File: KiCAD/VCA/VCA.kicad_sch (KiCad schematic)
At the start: 14 parts, among them J1 VIN, J2 VC, J3 VOUT, Q1 J172, Q2 J172, U1 LT1006

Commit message: VCA PCB Start
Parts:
- added J4: Conn_01x03_Pin, HackSynth:JST_PH_S3B-PH-K_1x03_P2.00mm_Horizontal, symbol Connector:Conn_01x03_Pin
- C1: footprint (none) -> Capacitor_THT:C_Disc_D5.0mm_W2.5mm_P5.00mm
- R1, R2, R3, R4: value ? -> 10k
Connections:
- net GND: now also J4.1 (Pin_1)
- net VDD: now also C1.1, J4.2 (Pin_2); no longer C1.2
- net VSS: now also C1.2, J4.3 (Pin_3)
- net at Q1.1 (D), R1.2, R3.1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: no longer C1.1
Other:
- note removed: "Is this an error in the original schematic?"
- note removed: "What are the resistor values?"
- moved on the sheet: C1, J1, J2, J3, Q1, Q2, R1, R3, R4, R5, RV1, RV2

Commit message: VCA PCB
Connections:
- net GND: now also J1.S, J2.S, J3.S
- no-connect marks 4 -> 1
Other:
- moved on the sheet: J3
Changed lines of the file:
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@@
+	)
+	(junction
+		(at 93.98 91.44)
+		(diameter 0)
+		(color 0 0 0 0)
+	)
+	(junction
+		(at 196.85 48.26)
+		(diameter 0)
+		(color 0 0 0 0)
 	)
 	(junction
@@
 	)
 	(junction
+		(at 93.98 60.96)
+		(diameter 0)
+		(color 0 0 0 0)
+	)
+	(junction
 		(at 154.94 53.34)
 		(diameter 0)
@@
 	)
 	(no_connect
-		(at 99.06 53.34)
-	)
-	(no_connect
-		(at 176.53 40.64)
-	)
-	(no_connect
-		(at 99.06 83.82)
-	)
-	(no_connect
 		(at 119.38 55.88)
 	)
@@
 	(wire
 		(pts
+			(xy 93.98 91.44) (xy 100.33 91.44)
+		)
+		(stroke
+			(width 0)
+			(type default)
+		)
+	)
+	(wire
+		(pts
+			(xy 167.64 43.18) (xy 191.77 43.18)
+		)
+		(stroke
+			(width 0)
+			(type default)
+		)
+	)
+	(wire
+		(pts
 			(xy 161.29 43.18) (xy 167.64 43.18)
 		)
@@
 	(wire
 		(pts
+			(xy 100.33 83.82) (xy 100.33 91.44)
+		)
+		(stroke
+			(width 0)
+			(type default)
+		)
+	)
+	(wire
+		(pts
 			(xy 191.77 92.71) (xy 191.77 101.6)
 		)
@@
 	(wire
 		(pts
+			(xy 99.06 83.82) (xy 100.33 83.82)
+		)
+		(stroke
+			(width 0)
+			(type default)
+		)
+	)
+	(wire
+		(pts
 			(xy 133.35 43.18) (xy 142.24 43.18)
 		)
@@
 	(wire
 		(pts
+			(xy 190.5 40.64) (xy 190.5 48.26)
+		)
+		(stroke
+			(width 0)
+			(type default)
+		)
+	)
+	(wire
+		(pts
 			(xy 142.24 43.18) (xy 153.67 43.18)
 		)
@@
 	(wire
 		(pts
-			(xy 167.64 43.18) (xy 176.53 43.18)
-		)
-		(stroke
-			(width 0)
-			(type default)
-		)
-	)
-	(wire
-		(pts
 			(xy 133.35 43.18) (xy 129.54 43.18)
 		)
@@
 	(wire
 		(pts
+			(xy 93.98 60.96) (xy 100.33 60.96)
+		)
+		(stroke
+			(width 0)
+			(type default)
+		)
+	)
+	(wire
+		(pts
 			(xy 154.94 76.2) (xy 154.94 73.66)
 		)
@@
 	(wire
 		(pts
-			(xy 181.61 48.26) (xy 181.61 52.07)
+			(xy 196.85 48.26) (xy 196.85 52.07)
 		)
 		(stroke
@@
 	(wire
 		(pts
+			(xy 99.06 53.34) (xy 100.33 53.34)
+		)
+		(stroke
+			(width 0)
+			(type default)
+		)
+	)
+	(wire
+		(pts
+			(xy 190.5 48.26) (xy 196.85 48.26)
+		)
+		(stroke
+			(width 0)
+			(type default)
+		)
+	)
+	(wire
+		(pts
 			(xy 104.14 43.18) (xy 104.14 55.88)
 		)
@@
 	(wire
 		(pts
+			(xy 191.77 40.64) (xy 190.5 40.64)
+		)
+		(stroke
+			(width 0)
+			(type default)
+		)
+	)
+	(wire
+		(pts
 			(xy 181.61 82.55) (xy 181.61 101.6)
+		)
+		(stroke
+			(width 0)
+			(type default)
+		)
+	)
+	(wire
+		(pts
+			(xy 100.33 53.34) (xy 100.33 60.96)
 		)
 		(stroke
@@
 	(symbol
 		(lib_id "power:GND")
-		(at 181.61 52.07 0)
+		(at 196.85 52.07 0)
 		(mirror y)
 		(unit 1)
@@
 		(fields_autoplaced yes)
 		(property "Reference" "#PWR09"
-			(at 181.61 58.42 0)
+			(at 196.85 58.42 0)
 			(effects
 				(font
@@
 		)
 		(property "Value" "GND"
-			(at 181.61 57.15 0)
+			(at 196.85 57.15 0)
 			(effects
 				(font
@@
 		)
 		(property "Footprint" ""
-			(at 181.61 52.07 0)
+			(at 196.85 52.07 0)
 			(effects
 				(font
@@
 		)
 		(property "Datasheet" ""
-			(at 181.61 52.07 0)
+			(at 196.85 52.07 0)
 			(effects
 				(font
@@
 		)
 		(property "Description" "Power symbol creates a global label with name \"GND\" , ground"
-			(at 181.61 52.07 0)
+			(at 196.85 52.07 0)
 			(effects
 				(font
@@
 	(symbol
 		(lib_id "HackSynth:AudioJack2_Ground")
-		(at 181.61 43.18 0)
+		(at 196.85 43.18 0)
 		(mirror y)
 		(unit 1)
@@
 		(dnp no)
 		(property "Reference" "J3"
-			(at 186.69 37.4649 0)
+			(at 201.93 37.4649 0)
 			(effects
 				(font
@@
 		)
 		(property "Value" "VOUT"
-			(at 186.69 43.8149 0)
+			(at 201.93 43.8149 0)
 			(effects
 				(font
@@
 		)
 		(property "Footprint" "HackSynth:Jack_3.5mm"
-			(at 181.61 43.18 0)
+			(at 196.85 43.18 0)
 			(effects
 				(font
@@
 		)
 		(property "Datasheet" "~"
-			(at 181.61 43.18 0)
+			(at 196.85 43.18 0)
 			(effects
 				(font
@@
 		)
 		(property "Description" "Audio Jack, 2 Poles (Mono / TS), Grounded Sleeve"
-			(at 181.61 43.18 0)
-			(effects
-				(font
+			(at 196.85 43.18 0)
+			(effects
+				(font

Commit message: VCA Footprint update
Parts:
- U1: footprint Package_DIP:DIP-8_W7.62mm -> HackSynth:DIP-8_W7.62mm_LongPads
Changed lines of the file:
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@@
 			)
 		)
-		(property "Footprint" "Package_DIP:DIP-8_W7.62mm"
+		(property "Footprint" "HackSynth:DIP-8_W7.62mm_LongPads"
 			(at 154.94 68.58 0)
 			(effects

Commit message: Backup Cleanup
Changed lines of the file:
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@@
 		(on_board yes)
 		(dnp no)
-		(fields_autoplaced yes)
 		(property "Reference" "R5"
-			(at 109.22 80.01 90)
+			(at 109.22 84.074 90)
 			(effects
 				(font
@@
 		)
 		(property "Value" "27k"
-			(at 109.22 82.55 90)
+			(at 109.22 86.36 90)
 			(effects
 				(font
@@
 		(on_board yes)
 		(dnp no)
-		(fields_autoplaced yes)
 		(property "Reference" "R4"
-			(at 171.45 76.2 90)
+			(at 171.45 80.264 90)
 			(effects
 				(font
@@
 		)
 		(property "Value" "10k"
-			(at 171.45 78.74 90)
+			(at 171.45 82.55 90)
 			(effects
 				(font
@@
 		(on_board yes)
 		(dnp no)
-		(fields_autoplaced yes)
 		(property "Reference" "R2"
-			(at 125.73 59.69 90)
+			(at 125.73 63.754 90)
 			(effects
 				(font
@@
 		)
 		(property "Value" "10k"
-			(at 125.73 62.23 90)
+			(at 125.73 66.04 90)
 			(effects
 				(font
@@
 		(dnp no)
 		(property "Reference" "R3"
-			(at 157.48 37.592 90)
+			(at 157.48 40.894 90)
 			(effects
 				(font
@@
 		)
 		(property "Value" "10k"
-			(at 157.48 40.132 90)
+			(at 157.48 43.18 90)
 			(effects
 				(font
@@
 		(dnp no)
 		(property "Reference" "R1"
-			(at 125.73 37.592 90)
+			(at 125.73 40.894 90)
 			(effects
 				(font
@@
 		)
 		(property "Value" "10k"
-			(at 125.73 40.132 90)
-			(effects
-				(font
+			(at 125.73 43.18 90)
+			(effects
+				(font

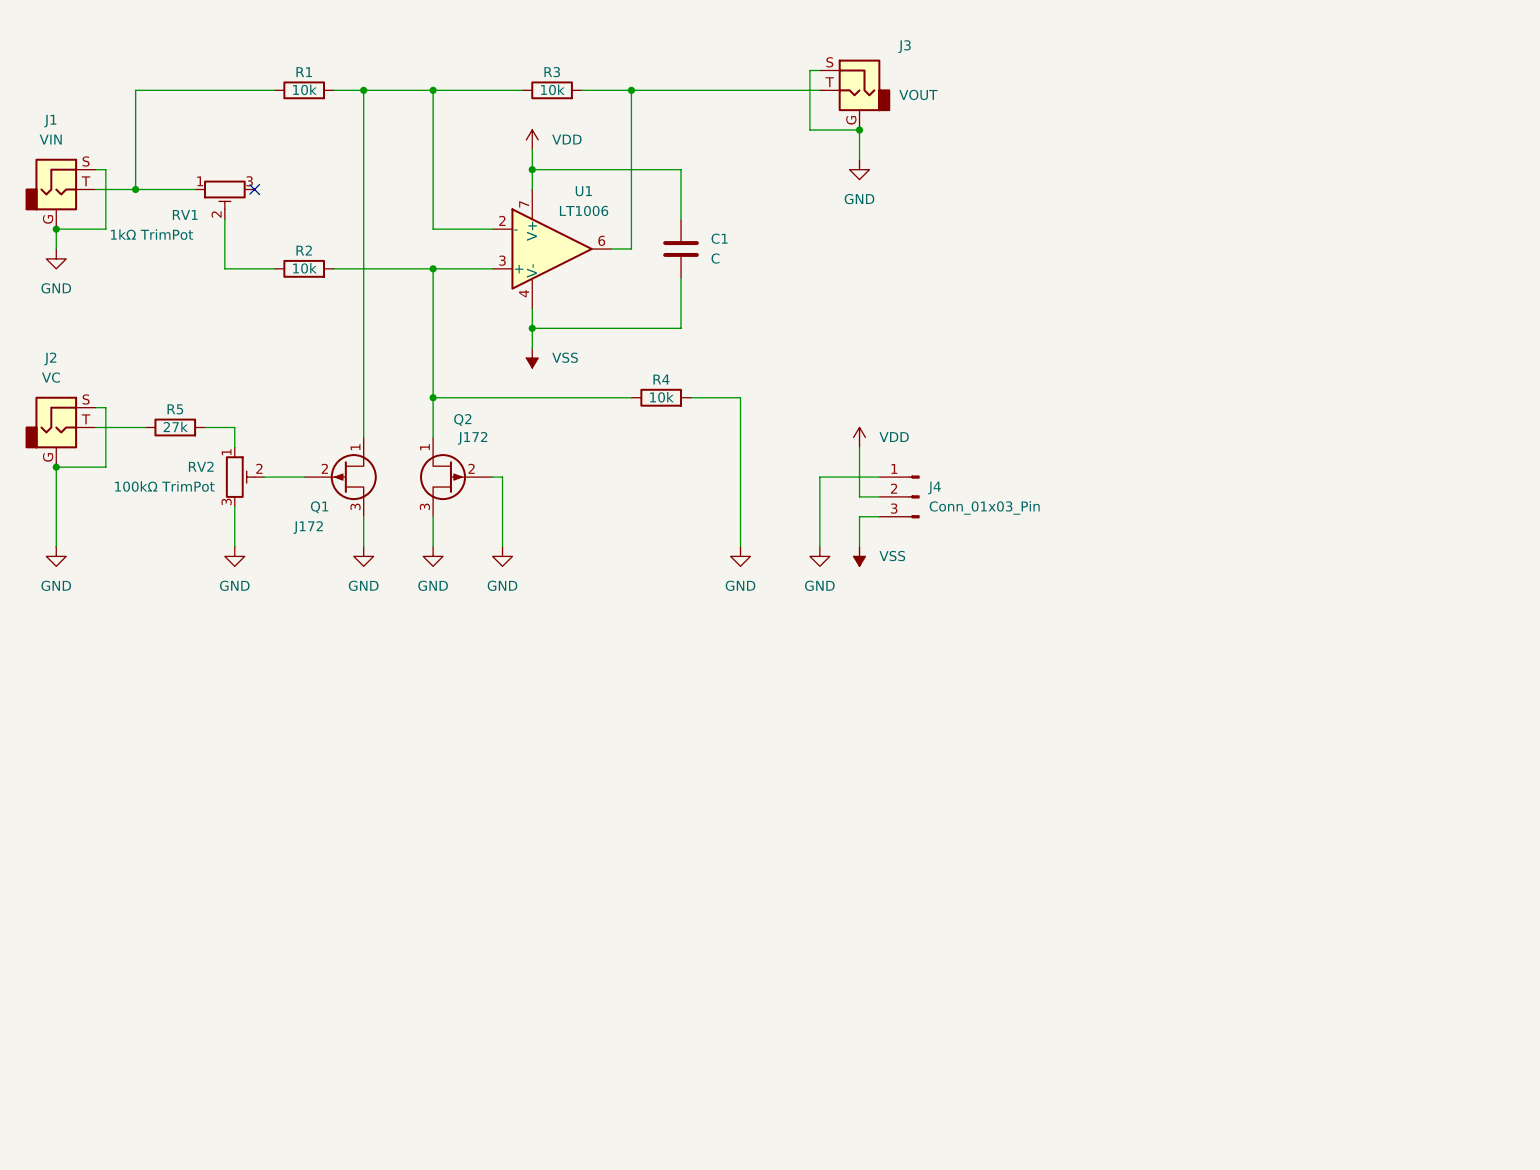
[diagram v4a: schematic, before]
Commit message: Footprint Edits
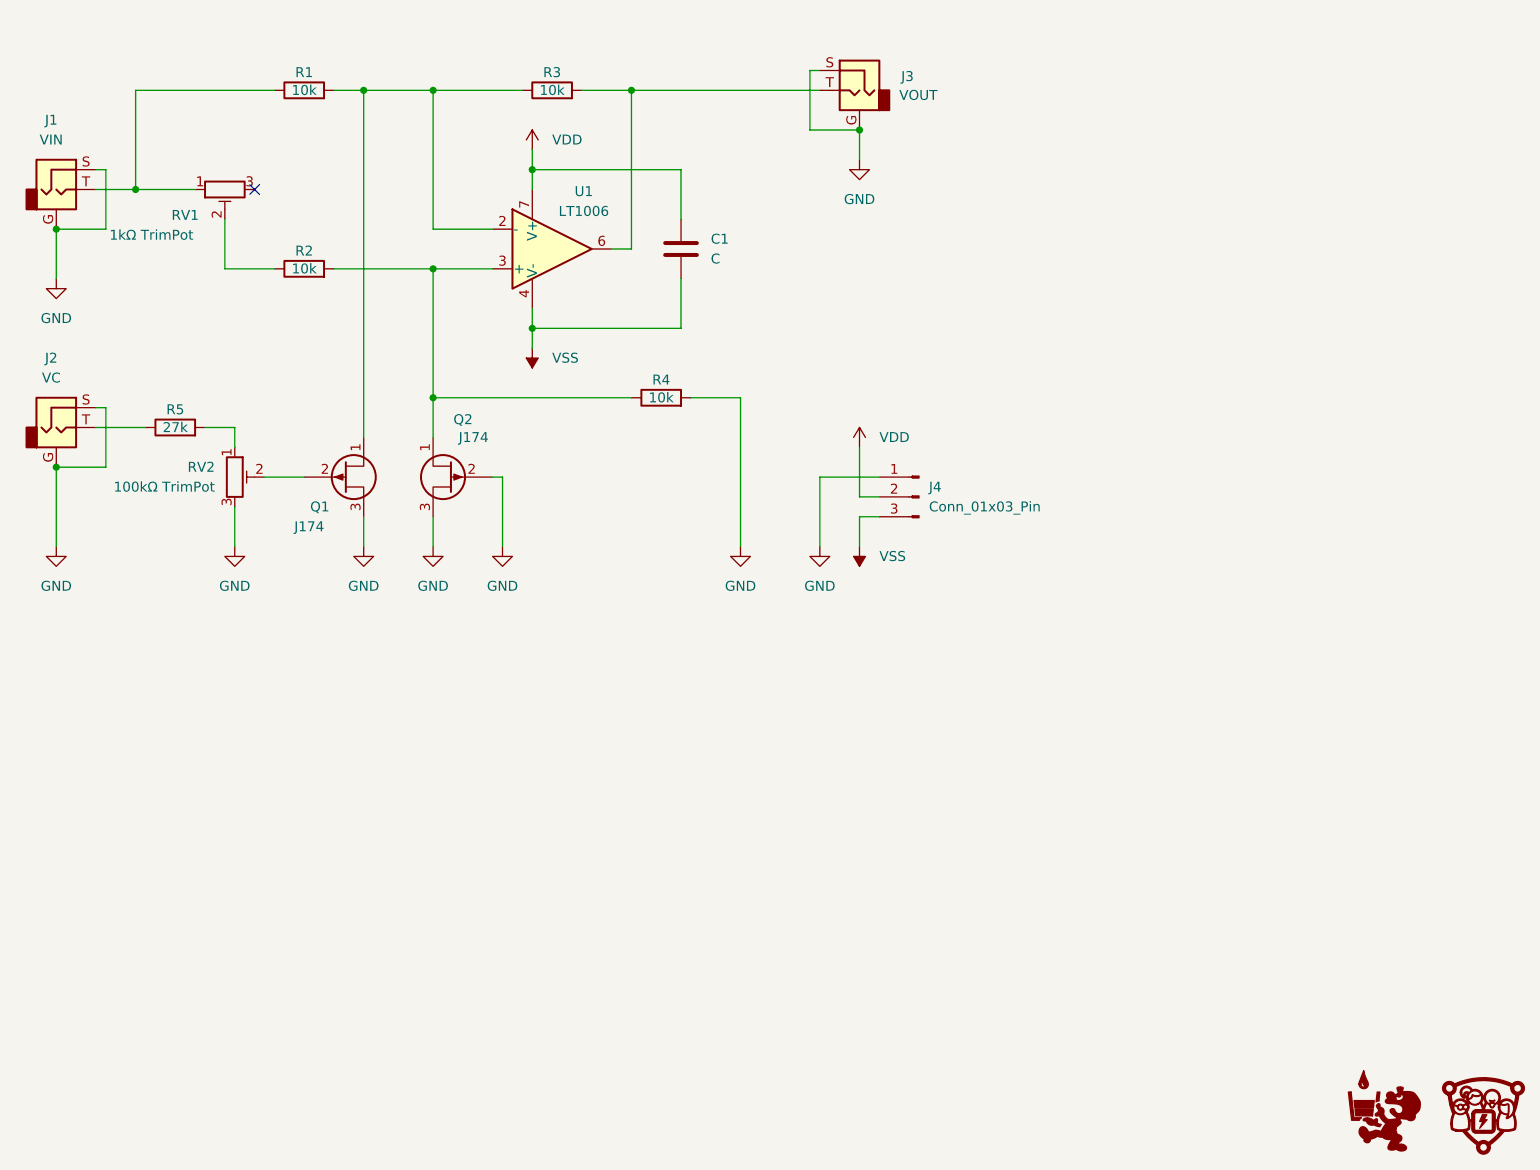
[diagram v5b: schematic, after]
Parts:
- added G1: ~, symbol HackSynth:CCHS_Logo
- added G2: ~, symbol HackSynth:Logo_PancakeLegend
- Q1, Q2: value J172 -> J174
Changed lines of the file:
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@@
 	(wire
 		(pts
-			(xy 93.98 63.5) (xy 93.98 60.96)
+			(xy 93.98 67.31) (xy 93.98 60.96)
 		)
 		(stroke
@@
 	)
 	(symbol
+		(lib_id "HackSynth:CCHS_Logo")
+		(at 276.86 173.355 0)
+		(unit 1)
+		(exclude_from_sim no)
+		(in_bom yes)
+		(on_board yes)
+		(dnp no)
+		(fields_autoplaced yes)
+		(property "Reference" "G1"
+			(at 276.86 180.975 0)
+			(effects
+				(font
+					(size 1.27 1.27)
+				)
+				(hide yes)
+			)
+		)
+		(property "Value" "~"
+			(at 283.21 174.525 0)
+			(effects
+				(font
+					(size 1.27 1.27)
+				)
+				(justify left)
+			)
+		)
+		(property "Footprint" ""
+			(at 276.86 173.355 0)
+			(effects
+				(font
+					(size 1.27 1.27)
+				)
+				(hide yes)
+			)
+		)
+		(property "Datasheet" ""
+			(at 276.86 173.355 0)
+			(effects
+				(font
+					(size 1.27 1.27)
+				)
+				(hide yes)
+			)
+		)
+		(property "Description" ""
+			(at 276.86 173.355 0)
+			(effects
+				(font
+					(size 1.27 1.27)
+				)
+				(hide yes)
+			)
+		)
+		(instances
+			(project "VCA"
+				(path "/aaf51f8b-ce1a-415b-85b4-b6a2b3e6a4a0"
+					(reference "G1")
+					(unit 1)
+				)
+			)
+		)
+	)
+	(symbol
 		(lib_id "HackSynth:J172_Q_PJFET_DGS")
 		(at 144.78 92.71 0)
@@
 			)
 		)
-		(property "Value" "J172"
+		(property "Value" "J174"
 			(at 149.352 87.63 0)
 			(effects
@@
 			)
 		)
-		(property "Value" "J172"
+		(property "Value" "J174"
 			(at 124.46 99.06 0)
 			(effects
@@
 	(symbol
 		(lib_id "power:GND")
-		(at 93.98 63.5 0)
+		(at 93.98 67.31 0)
 		(unit 1)
 		(exclude_from_sim no)
@@
 		(fields_autoplaced yes)
 		(property "Reference" "#PWR03"
-			(at 93.98 69.85 0)
+			(at 93.98 73.66 0)
 			(effects
 				(font
@@
 		)
 		(property "Value" "GND"
-			(at 93.98 68.58 0)
+			(at 93.98 72.39 0)
 			(effects
 				(font
@@
 		)
 		(property "Footprint" ""
-			(at 93.98 63.5 0)
+			(at 93.98 67.31 0)
 			(effects
 				(font
@@
 		)
 		(property "Datasheet" ""
-			(at 93.98 63.5 0)
+			(at 93.98 67.31 0)
 			(effects
 				(font
@@
 		)
 		(property "Description" "Power symbol creates a global label with name \"GND\" , ground"
-			(at 93.98 63.5 0)
+			(at 93.98 67.31 0)
 			(effects
 				(font
@@
 		(dnp no)
 		(property "Reference" "J3"
-			(at 201.93 37.4649 0)
+			(at 202.184 41.402 0)
 			(effects
 				(font
@@
 					(unit 1)
 				)
+			)
+		)
+	)
+	(symbol
+		(lib_id "HackSynth:Logo_PancakeLegend")
+		(at 264.16 173.99 0)
+		(unit 1)
+		(exclude_from_sim no)
+		(in_bom yes)
+		(on_board yes)
+		(dnp no)
+		(fields_autoplaced yes)
+		(property "Reference" "G2"
+			(at 264.16 181.61 0)
+			(effects
+				(font
+					(size 1.27 1.27)
+				)
+				(hide yes)
+			)
+		)
+		(property "Value" "~"
+			(at 270.51 173.8899 0)
+			(effects
+				(font
+					(size 1.27 1.27)
+				)
+				(justify left)
+			)
+		)
+		(property "Footprint" ""
+			(at 264.16 173.99 0)
+			(effects
+				(font
+					(size 1.27 1.27)
+				)
+				(hide yes)
+			)
+		)
+		(property "Datasheet" ""
+			(at 264.16 173.99 0)
+			(effects
+				(font
+					(size 1.27 1.27)
+				)
+				(hide yes)
+			)
+		)
+		(property "Description" ""
+			(at 264.16 173.99 0)
+			(effects
+				(font
+					(size 1.27 1.27)
+				)
+				(hide yes)
+			)
+		)
+		(instances
+			(project "VCA"
+				(path "/aaf51f8b-ce1a-415b-85b4-b6a2b3e6a4a0"
+					(reference "G2")
+					(unit 1)
+				)
